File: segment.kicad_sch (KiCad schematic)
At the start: 9 parts, among them Q5 MBT3904DW1, Q6 IRLML6346

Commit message: production ready
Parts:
- added R55: 100k, Resistor_SMD:R_0603_1608Metric, symbol Device:R
- D13: renamed from D7; DigiKey# (none) -> 160-1427-1-ND
- D14: renamed from D8; DigiKey# (none) -> 160-1427-1-ND
- D15: renamed from D9; DigiKey# (none) -> 160-1427-1-ND
- Q10: renamed from Q6; value IRLML6346 -> T2N7002AK,LM; DigiKey# IRLML6346TRPBFCT-ND -> (none); Mouser# (none) -> 757-T2N7002AKLM
- Q9: renamed from Q5; DigiKey# (none) -> MBT3904DW1T3GOSCT-ND
- R14: renamed from R8; value 10 -> 1k; Mouser# (none) -> 791-RMC1/16-100JTP
- R15: renamed from R9; Mouser# (none) -> 603-RC0603FR-0736RL
- renumbered R7 to R13
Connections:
- net Enable: now also R55.2
- net GND: now also R55.1
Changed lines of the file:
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@@
 (kicad_sch (version 20211123) (generator eeschema)
   (paper "A4")
+  (junction (at 131.445 105.41) (diameter 0) (color 0 0 0 0)
+  )
   (junction (at 133.35 80.01) (diameter 0) (color 0 0 0 0)
   )
@@
     (stroke (width 0) (type default) (color 0 0 0 0))
   )
+  (wire (pts (xy 131.445 105.41) (xy 133.35 105.41))
+    (stroke (width 0) (type default) (color 0 0 0 0))
+  )
   (wire (pts (xy 131.445 55.88) (xy 133.35 55.88))
     (stroke (width 0) (type default) (color 0 0 0 0))
   )
-  (wire (pts (xy 131.445 105.41) (xy 133.35 105.41))
+  (wire (pts (xy 129.54 105.41) (xy 131.445 105.41))
+    (stroke (width 0) (type default) (color 0 0 0 0))
+  )
+  (wire (pts (xy 131.445 114.935) (xy 131.445 116.84))
     (stroke (width 0) (type default) (color 0 0 0 0))
   )
@@
     (stroke (width 0) (type default) (color 0 0 0 0))
   )
+  (wire (pts (xy 131.445 105.41) (xy 131.445 107.315))
+    (stroke (width 0) (type default) (color 0 0 0 0))
+  )
   (wire (pts (xy 150.495 73.025) (xy 150.495 74.93))
     (stroke (width 0) (type default) (color 0 0 0 0))
@@
     (stroke (width 0) (type default) (color 0 0 0 0))
   )
-  (hierarchical_label "Enable" (shape input) (at 131.445 105.41 180)
+  (hierarchical_label "Enable" (shape input) (at 129.54 105.41 180)
     (effects (font (size 1.27 1.27)) (justify right))
   )
@@
   (symbol (lib_id "Device:R") (at 133.35 69.215 0)
     (in_bom yes) (on_board yes)
-    (property "Reference" "R7" (id 0) (at 128.27 68.58 0)
+    (property "Reference" "R13" (id 0) (at 128.27 68.58 0)
       (effects (font (size 1.27 1.27)) (justify left))
     )
@@
   (symbol (lib_id "Device:LED") (at 144.78 73.025 180)
     (in_bom yes) (on_board yes)
-    (property "Reference" "D9" (id 0) (at 144.78 69.85 0))
+    (property "Reference" "D15" (id 0) (at 144.78 69.85 0))
     (property "Value" "LTST-C171KRKT " (id 1) (at 160.655 73.025 0)
       (effects (font (size 1.27 1.27)) hide)
@@
       (effects (font (size 1.27 1.27)) hide)
     )
+    (property "DigiKey#" "160-1427-1-ND" (id 5) (at 144.78 73.025 0)
+      (effects (font (size 1.27 1.27)) hide)
+    )
     (pin "1")
     (pin "2")
@@
   (symbol (lib_id "Device:LED") (at 144.78 65.405 0)
     (in_bom yes) (on_board yes)
-    (property "Reference" "D8" (id 0) (at 144.78 62.23 0))
+    (property "Reference" "D14" (id 0) (at 144.78 62.23 0))
     (property "Value" "LTST-C171KRKT " (id 1) (at 153.035 64.77 90))
     (property "Footprint" "LED_SMD:LED_0805_2012Metric" (id 2) (at 144.78 65.405 0)
@@
       (effects (font (size 1.27 1.27)) hide)
     )
+    (property "DigiKey#" "160-1427-1-ND" (id 5) (at 144.78 65.405 0)
+      (effects (font (size 1.27 1.27)) hide)
+    )
     (pin "1")
     (pin "2")
@@
   (symbol (lib_id "Device:LED") (at 144.78 58.42 180)
     (in_bom yes) (on_board yes)
-    (property "Reference" "D7" (id 0) (at 144.78 55.245 0))
+    (property "Reference" "D13" (id 0) (at 144.78 55.245 0))
     (property "Value" "LTST-C171KRKT " (id 1) (at 161.925 55.88 0)
       (effects (font (size 1.27 1.27)) hide)
@@
       (effects (font (size 1.27 1.27)) hide)
     )
+    (property "DigiKey#" "160-1427-1-ND" (id 5) (at 144.78 58.42 0)
+      (effects (font (size 1.27 1.27)) hide)
+    )
     (pin "1")
     (pin "2")
@@
   (symbol (lib_id "Device:R") (at 137.16 105.41 90)
     (in_bom yes) (on_board yes) (fields_autoplaced)
-    (property "Reference" "R8" (id 0) (at 137.16 100.6942 90))
-    (property "Value" "10" (id 1) (at 137.16 103.2311 90))
+    (property "Reference" "R14" (id 0) (at 137.16 100.6942 90))
+    (property "Value" "1k" (id 1) (at 137.16 103.2311 90))
     (property "Footprint" "Resistor_SMD:R_0603_1608Metric" (id 2) (at 137.16 107.188 90)
       (effects (font (size 1.27 1.27)) hide)
@@
       (effects (font (size 1.27 1.27)) hide)
     )
+    (property "Mouser#" "791-RMC1/16-100JTP " (id 4) (at 137.16 105.41 0)
+      (effects (font (size 1.27 1.27)) hide)
+    )
     (pin "1")
     (pin "2")
@@
   (symbol (lib_id "Device:Q_NMOS_GSD") (at 147.955 105.41 0)
     (in_bom yes) (on_board yes)
-    (property "Reference" "Q6" (id 0) (at 153.162 104.5753 0)
-      (effects (font (size 1.27 1.27)) (justify left))
-    )
-    (property "Value" "IRLML6346" (id 1) (at 139.065 109.855 0)
+    (property "Reference" "Q10" (id 0) (at 153.162 104.5753 0)
+      (effects (font (size 1.27 1.27)) (justify left))
+    )
+    (property "Value" "T2N7002AK,LM" (id 1) (at 153.035 106.68 0)
       (effects (font (size 1.27 1.27)) (justify left))
     )
@@
       (effects (font (size 1.27 1.27)) hide)
     )
-    (property "Datasheet" "https://www.infineon.com/dgdl/irlml6346pbf.pdf?fileId=5546d462533600a401535668a336262e" (id 3) (at 147.955 105.41 0)
-      (effects (font (size 1.27 1.27)) hide)
-    )
-    (property "DigiKey#" "IRLML6346TRPBFCT-ND" (id 4) (at 147.955 105.41 0)
+    (property "Datasheet" "https://www.mouser.de/datasheet/2/408/T2N7002AK_datasheet_en_20150401-1916411.pdf" (id 3) (at 147.955 105.41 0)
+      (effects (font (size 1.27 1.27)) hide)
+    )
+    (property "DigiKey#" "" (id 4) (at 147.955 105.41 0)
+      (effects (font (size 1.27 1.27)) hide)
+    )
+    (property "Mouser#" "757-T2N7002AKLM" (id 5) (at 147.955 105.41 0)
       (effects (font (size 1.27 1.27)) hide)
     )
@@
   (symbol (lib_id "Transistor_BJT:MBT3904DW1") (at 135.89 86.995 0) (mirror y)
     (in_bom yes) (on_board yes)
-    (property "Reference" "Q5" (id 0) (at 130.81 86.995 0)
+    (property "Reference" "Q9" (id 0) (at 130.81 86.995 0)
       (effects (font (size 1.27 1.27)) (justify left))
     )
@@
     )
     (property "Mouser#" "863-MBT3904DW1T3G" (id 4) (at 135.89 86.995 0)
+      (effects (font (size 1.27 1.27)) hide)
+    )
+    (property "DigiKey#" "MBT3904DW1T3GOSCT-ND" (id 5) (at 135.89 86.995 0)
       (effects (font (size 1.27 1.27)) hide)
     )
@@
   (symbol (lib_id "Device:R") (at 150.495 92.71 0)
     (in_bom yes) (on_board yes) (fields_autoplaced)
-    (property "Reference" "R9" (id 0) (at 152.273 91.8753 0)
+    (property "Reference" "R15" (id 0) (at 152.273 91.8753 0)
       (effects (font (size 1.27 1.27)) (justify left))
     )
@@
       (effects (font (size 1.27 1.27)) hide)
     )
+    (property "Mouser#" "603-RC0603FR-0736RL" (id 4) (at 150.495 92.71 0)
+      (effects (font (size 1.27 1.27)) hide)
+    )
     (pin "1")
     (pin "2")
@@
   (symbol (lib_id "Transistor_BJT:MBT3904DW1") (at 147.955 80.01 0)
     (in_bom yes) (on_board yes)
-    (property "Reference" "Q5" (id 0) (at 152.4 80.01 0)
+    (property "Reference" "Q9" (id 0) (at 152.4 80.01 0)
       (effects (font (size 1.27 1.27)) (justify left))
     )
@@
       (effects (font (size 1.27 1.27)) hide)
     )
+    (property "DigiKey#" "MBT3904DW1T3GOSCT-ND" (id 5) (at 147.955 80.01 0)
+      (effects (font (size 1.27 1.27)) hide)
+    )
     (pin "1")
     (pin "2")
@@
   (symbol (lib_id "power:GND") (at 150.495 112.395 0)
     (in_bom yes) (on_board yes) (fields_autoplaced)
-    (property "Reference" "#PWR020" (id 0) (at 150.495 118.745 0)
+    (property "Reference" "#PWR022" (id 0) (at 150.495 118.745 0)
       (effects (font (size 1.27 1.27)) hide)
     )
@@
     (pin "1")
   )
+  (symbol (lib_id "power:GND") (at 131.445 116.84 0)
+    (in_bom yes) (on_board yes) (fields_autoplaced)
+    (property "Reference" "#PWR064" (id 0) (at 131.445 123.19 0)
+      (effects (font (size 1.27 1.27)) hide)
+    )
+    (property "Value" "GND" (id 1) (at 131.445 121.2834 0))
+    (property "Footprint" "" (id 2) (at 131.445 116.84 0)
+      (effects (font (size 1.27 1.27)) hide)
+    )
+    (property "Datasheet" "" (id 3) (at 131.445 116.84 0)
+      (effects (font (size 1.27 1.27)) hide)
+    )
+    (pin "1")
+  )
+  (symbol (lib_id "Device:R") (at 131.445 111.125 180)
+    (in_bom yes) (on_board yes) (fields_autoplaced)
+    (property "Reference" "R55" (id 0) (at 133.223 110.2903 0)
+      (effects (font (size 1.27 1.27)) (justify right))
+    )
+    (property "Value" "100k" (id 1) (at 133.223 112.8272 0)
+      (effects (font (size 1.27 1.27)) (justify right))
+    )
+    (property "Footprint" "Resistor_SMD:R_0603_1608Metric" (id 2) (at 133.223 111.125 90)
+      (effects (font (size 1.27 1.27)) hide)
+    )
+    (property "Datasheet" "~" (id 3) (at 131.445 111.125 0)
+      (effects (font (size 1.27 1.27)) hide)
+    )
+    (property "Mouser#" "791-RMC1/16-100JTP " (id 4) (at 131.445 111.125 0)
+      (effects (font (size 1.27 1.27)) hide)
+    )
+    (pin "1")
+    (pin "2")
+  )
 )

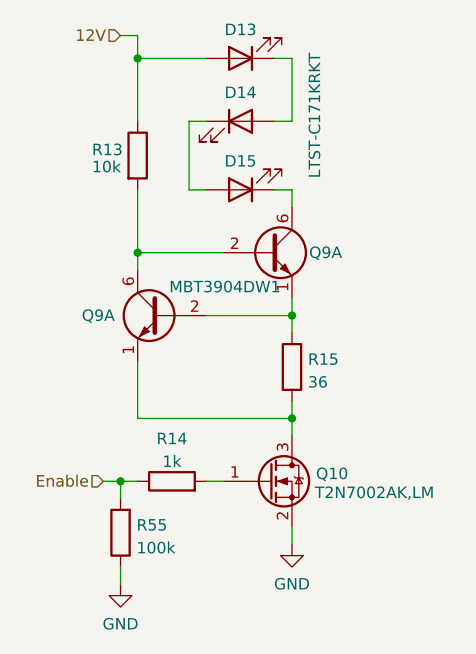
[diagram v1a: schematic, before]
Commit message: 7.0.1 -> 7.0.10
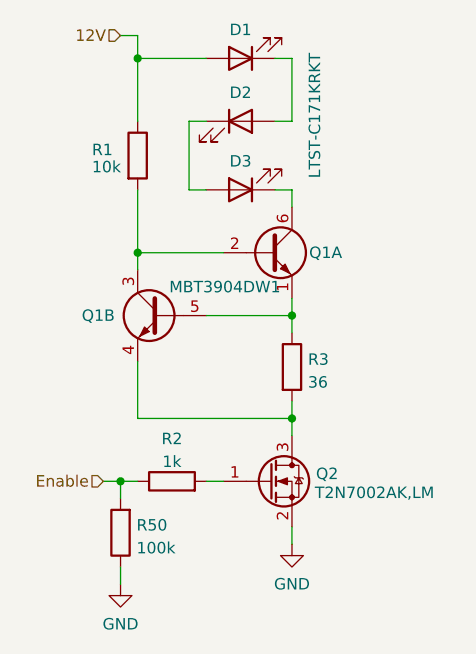
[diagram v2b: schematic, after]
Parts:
- renumbered D13 to D1, D14 to D2, D15 to D3, Q9 to Q1, Q10 to Q2, R13 to R1, R14 to R2, R15 to R3, R55 to R50
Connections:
- net at Q1.2 (B1), R1.2: now also Q1.3 (C2); no longer Q1.6 (C1)
- net at Q2.3 (D), R3.2: now also Q1.4 (E2); no longer Q1.1 (E1)
- net at Q1.1 (E1), R3.1: now also Q1.5 (B2); no longer Q1.2 (B1)
